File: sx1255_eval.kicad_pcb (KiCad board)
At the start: 2 copper layers, 26 parts, among them IC1 SX1255, J1 EXT_CLK_IN, J2 TX_SMA, J3 RX_SMA, J4 CONN

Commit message: WIP PCB layout
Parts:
- moved R9 44.7 mm to (159.5, 90.9), turned to 180 degrees
- moved R8 44.2 mm to (159.5, 89.4), turned to 180 degrees
- moved R7 43.6 mm to (159.5, 87.9), turned to 180 degrees
- moved R2 36.1 mm to (148.8, 96.5), turned to -90 degrees
- moved R6 34.3 mm to (154.9, 96.5), turned to -90 degrees
- moved R1 33.4 mm to (147.3, 96.5), turned to -90 degrees
- moved R5 32.0 mm to (153.4, 96.5), turned to -90 degrees
- moved R4 29.8 mm to (151.9, 96.5), turned to -90 degrees
- moved R3 27.7 mm to (150.4, 96.5), turned to -90 degrees
- moved J1 19.2 mm to (142.5, 90.9), turned to 90 degrees
- moved L1 12.1 mm to (129.8, 115.3)
- moved L2 8.03 mm to (126.5, 115.3)
- moved J4 4.61 mm to (168.2, 82.5)
- moved IC1 0.67 mm to (150.9, 89.2)
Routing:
- net CK_OUT: track 0.00 -> 57.2 mm
- net CK_IN: track 0.00 -> 51.9 mm
- net Q_IN: track 0.00 -> 46.6 mm
- net I_IN: track 0.00 -> 41.1 mm
- net Q_OUT: track 0.00 -> 35.8 mm
- net I_OUT: track 0.00 -> 30.4 mm
- net DIO3: track 0.00 -> 19.2 mm
- net DIO2: track 0.00 -> 17.3 mm
- net DIO1: track 0.00 -> 15.9 mm
- net DIO0: track 0.00 -> 15.0 mm
- net ~{CS}: track 0.00 -> 14.2 mm
- net Net-(IC1-MOSI): track 0.00 -> 6.24 mm
- net SCK: track 0.00 -> 6.09 mm
- net Net-(IC1-MISO): track 0.00 -> 5.81 mm
- net MISO: track 0.00 -> 5.66 mm
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
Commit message: WIP PCB
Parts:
- added C1: 10n, Capacitor_SMD:C_0603_1608Metric, F.Cu at (142.7, 87.1)
- added C6: 100n, Capacitor_SMD:C_0603_1608Metric, F.Cu at (159.5, 94.0)
- moved C3 45.9 mm to (159.5, 92.5)
- moved C12 43.4 mm to (154.7, 82.0), turned to 90 degrees
- moved L2 41.7 mm to (151.6, 82.0), turned to -90 degrees
- moved C5 40.9 mm to (145.5, 82.0), turned to 90 degrees
- moved L1 40.7 mm to (153.2, 82.0), turned to -90 degrees
- moved C7 39.2 mm to (142.7, 84.1), turned to 180 degrees
- moved C9 38.5 mm to (142.7, 90.2), turned to 180 degrees
- moved C11 38.2 mm to (150.1, 82.0), turned to 90 degrees
- moved C8 37.8 mm to (142.7, 88.6), turned to 180 degrees
- moved C2 37.6 mm to (147.1, 82.0), turned to 90 degrees
- moved C10 35.5 mm to (148.6, 82.0), turned to 90 degrees
- moved C4 34.9 mm to (142.7, 85.6), turned to 180 degrees
- moved J3 33.7 mm to (156.2, 71.0), turned to 180 degrees
- moved J2 28.8 mm to (141.0, 71.0), turned to 180 degrees
- moved J1 4.60 mm to (143.0, 95.5), turned to 180 degrees
- renumbered C8 to C10, C9 to C11, C10 to C12, C1 to C2, C2 to C3, C3 to C4, C4 to C5, C5 to C7, C6 to C8, C7 to C9
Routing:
- net RST: track 0.00 -> 69.1 mm
- net +3V3: track 0.00 -> 56.4 mm, vias 0 -> 4
- net Net-(J2-In): track 0.00 -> 13.6 mm
- net Net-(J3-In): track 0.00 -> 12.3 mm
- net EXT_CLK: track 0.00 -> 7.13 mm
- net Net-(IC1-VR_PA): track 0.00 -> 6.32 mm
- net Net-(IC1-RFI): track 0.00 -> 5.52 mm
- net Net-(IC1-VR_DIG): track 0.00 -> 5.18 mm
- net Net-(IC1-VR_ANAI): track 0.00 -> 4.96 mm
- net Net-(IC1-VR_ANA2): track 0.00 -> 4.86 mm
- net Net-(IC1-RFO_P): track 0.00 -> 4.64 mm
- net Net-(IC1-RFO_N): track 0.00 -> 4.22 mm
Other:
- board outline added: 43 x 34 mm

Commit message: PCB cleanup
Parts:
- moved R7 3.31 mm to (159.3, 91.2)
- moved C3 3.31 mm to (159.3, 95.8)
- moved C6 3.31 mm to (159.3, 97.3)
- moved R8 3.31 mm to (159.3, 92.7)
- moved R9 3.31 mm to (159.3, 94.2)
- moved J4 3.05 mm to (168.2, 85.6)
- moved J2 3.03 mm to (144.0, 71.0)
- moved J3 0.18 mm to (156.0, 71.0)
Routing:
- net DIO3: track 19.2 -> 16.3 mm
- net DIO2: track 17.3 -> 15.4 mm
- net RST: track 69.1 -> 67.4 mm
- net CK_OUT: track 57.2 -> 55.4 mm
- net CK_IN: track 51.9 -> 50.1 mm
- net Q_IN: track 46.6 -> 44.8 mm
- net I_IN: track 41.1 -> 39.3 mm
- net Q_OUT: track 35.8 -> 34.0 mm
- net I_OUT: track 30.4 -> 28.7 mm
- net +3V3: track 56.4 -> 54.7 mm
- net Net-(J2-In): track 13.6 -> 12.1 mm
- net DIO1: track 15.9 -> 14.6 mm
- net ~{CS}: track 14.2 -> 12.9 mm
- net DIO0: track 15.0 -> 13.7 mm
- net Net-(IC1-SCK): track 5.39 -> 6.54 mm
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- added copper zone on B.Cu, net GND
- added copper zone on F.Cu, net GND
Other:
- board text added: "3V3"
- board text added: "CK_IN"
- board text added: "CK_OUT"
- board text added: "EXT REF"
- board text added: "GND"
- board text added: "IO0"
- board text added: "IO1"
- board text added: "IO2"
- board text added: "IO3"
- board text added: "I_IN"
- board text added: "MISO"
- board text added: "MOSI"
- board text added: "Q_IN"
- board text added: "Q_OUT"
- board text added: "RST"
- board text added: "RX"
- board text added: "SCK"
- board text added: "SX1255 Minimalistic Evaluation Board"
- board text added: "TX"
- board text added: "Wojciech SP5WWP M17 Project 2023"
- board text added: "~{CS}"

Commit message: PMOD
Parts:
- added J5: PMOD, Connector_PinHeader_2.54mm:PinHeader_2x06_P2.54mm_Horizontal, F.Cu at (165.6, 94.5)
- added JP1: EXT_CLK_SRC, Connector_PinHeader_2.54mm:PinHeader_1x03_P2.54mm_Vertical, F.Cu at (145.5, 107.2)
- added REF**: OSHW-Logo2_7.3x6mm_SilkScreen, Symbol:OSHW-Logo2_7.3x6mm_SilkScreen, F.Cu at (140.7, 96.3)
- J1: footprint Connector_Coaxial:U.FL_Molex_MCRF_73412-0110_Vertical -> Connector_Coaxial:SMA_Samtec_SMA-J-P-X-ST-EM1_EdgeMount
- J4: value CONN -> PMOD; footprint Connector_PinHeader_2.54mm:PinHeader_2x09_P2.54mm_Vertical_SMD -> Connector_PinHeader_2.54mm:PinHeader_2x06_P2.54mm_Horizontal
- moved J3 22.5 mm to (134.1, 76.0), turned to -90 degrees
- moved J2 21.0 mm to (134.1, 89.5), turned to -90 degrees
- moved J4 14.2 mm to (165.6, 71.6)
- moved J1 11.6 mm to (134.1, 103.0), turned to -90 degrees
- moved C3 2.90 mm to (156.5, 96.5), turned to -90 degrees
- moved R7 2.54 mm to (159.3, 88.6)
- moved R8 2.54 mm to (159.3, 90.2)
- moved R9 2.54 mm to (159.3, 91.7)
- moved C7 1.48 mm to (158.0, 96.5), turned to -90 degrees
- renumbered C7 to C6, C6 to C7
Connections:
- net Net-(J2-In) renamed /RF_OUT
- net Net-(J3-In) renamed /RF_IN
- J1 pad 1: EXT_CLK -> EXT_CLK_B
- J4 pad 10: I_IN -> MISO
- J4 pad 11: ~{CS} -> MOSI
- J4 pad 12: Q_OUT -> SCK
- J4 pad 2: RST -> +3V3
- J4 pad 3: DIO3 -> GND
- J4 pad 4: CK_OUT -> GND
- J4 pad 5: DIO2 -> DIO3
- J4 pad 6: CK_IN -> DIO2
- J4 pad 8: Q_IN -> DIO0
- J4 pad 9: DIO0 -> ~{CS}
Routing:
- net RST: track 67.4 -> 31.1 mm
- net CK_OUT: track 55.4 -> 25.5 mm
- net CK_IN: track 50.1 -> 20.3 mm
- net Q_IN: track 44.8 -> 21.4 mm
- net I_IN: track 39.3 -> 16.1 mm
- net EXT_CLK_A: track 0.00 -> 18.6 mm
- net +3V3: track 54.7 -> 72.2 mm, vias 4 -> 3
- net Q_OUT: track 34.0 -> 17.1 mm
- net I_OUT: track 28.7 -> 12.0 mm
- net EXT_CLK_B: track 0.00 -> 13.4 mm
- net GND: track 0.00 -> 12.2 mm, vias 69 -> 186
- net /RF_OUT: track 12.1 -> 24.2 mm
- net EXT_CLK: track 7.13 -> 18.8 mm
- net /RF_IN: track 12.0 -> 21.1 mm
- net MISO: track 5.77 -> 12.7 mm
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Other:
- board size 43 x 34 mm -> 40 x 41 mm
- board text added: "EXT REF SEL"
- board text added: "I_OUT"
- board text added: "OUT"
- board text added: "REF"
- board text added: "SX1255 Minimalistic Evaluation Board M17 Project, December 2023 Wojciech SP5WWP"
- board text removed: "3V3"
- board text removed: "CK_OUT"
- board text removed: "GND"
- board text removed: "SX1255 Minimalistic Evaluation Board"
- board text removed: "Wojciech SP5WWP M17 Project 2023"

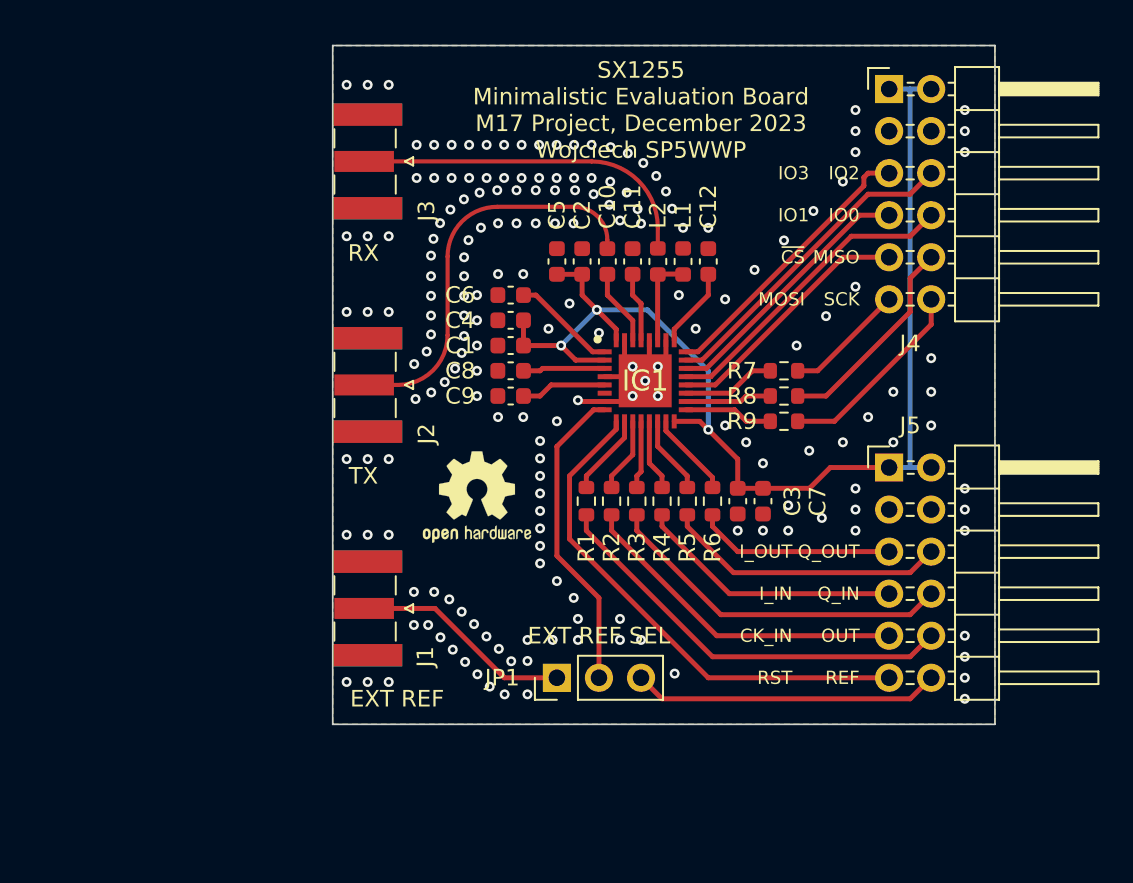
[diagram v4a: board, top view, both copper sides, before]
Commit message: changed PCB orientation
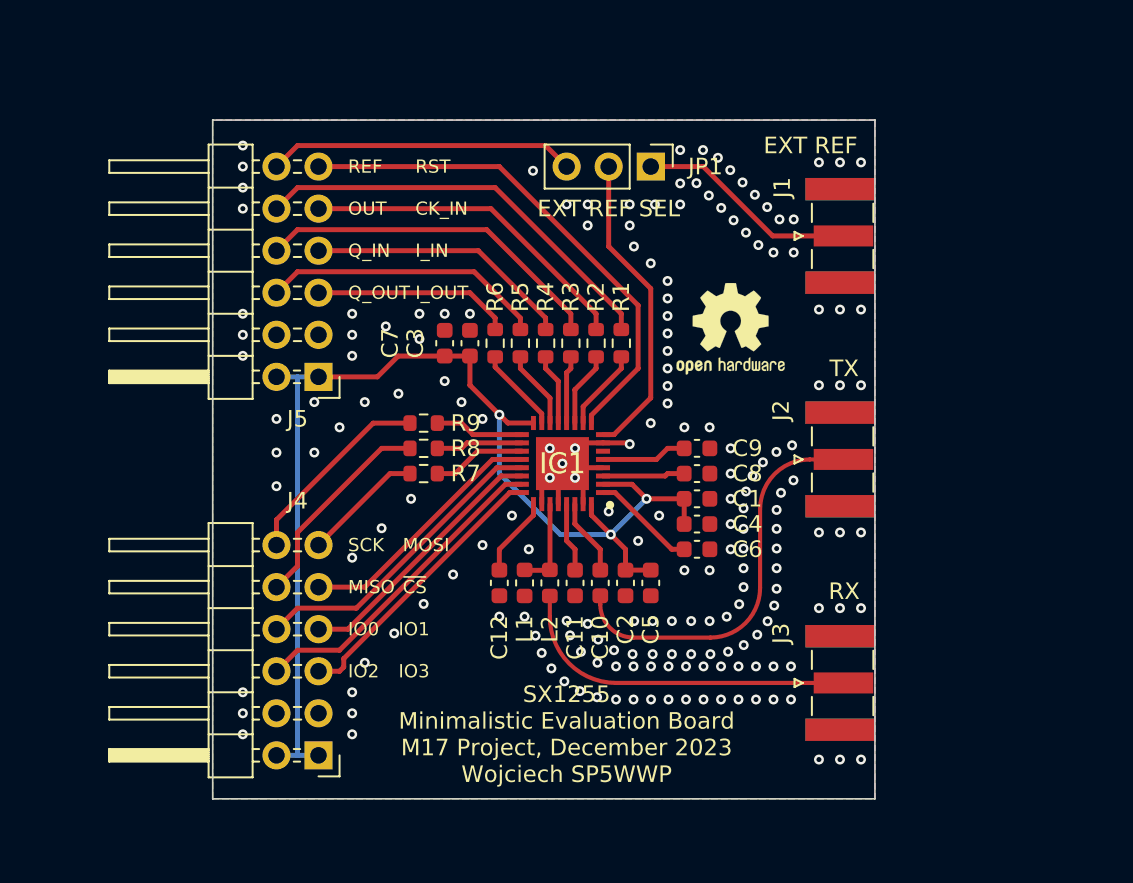
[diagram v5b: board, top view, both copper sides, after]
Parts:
- moved J4 53.0 mm to (131.1, 111.9), turned to 180 degrees
- moved J3 42.5 mm to (162.7, 107.5), turned to 90 degrees
- moved J1 36.4 mm to (162.7, 80.5), turned to 90 degrees
- moved J5 34.9 mm to (131.1, 89.0), turned to 180 degrees
- moved JP1 31.4 mm to (151.2, 76.3), turned to -90 degrees
- moved J2 28.9 mm to (162.7, 94.0), turned to 90 degrees
- moved C12 23.2 mm to (142.1, 101.5), turned to -90 degrees
- moved R7 22.6 mm to (137.5, 94.9), turned to 0 degrees
- moved R8 22.0 mm to (137.5, 93.3), turned to 0 degrees
- moved R9 21.8 mm to (137.5, 91.8), turned to 0 degrees
- moved L1 21.6 mm to (143.6, 101.5), turned to 90 degrees
- moved C7 21.5 mm to (138.8, 87.0), turned to 90 degrees
- moved L2 20.5 mm to (145.1, 101.5), turned to 90 degrees
- moved C5 20.2 mm to (151.2, 101.5), turned to -90 degrees
- moved C11 19.7 mm to (146.6, 101.5), turned to -90 degrees
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
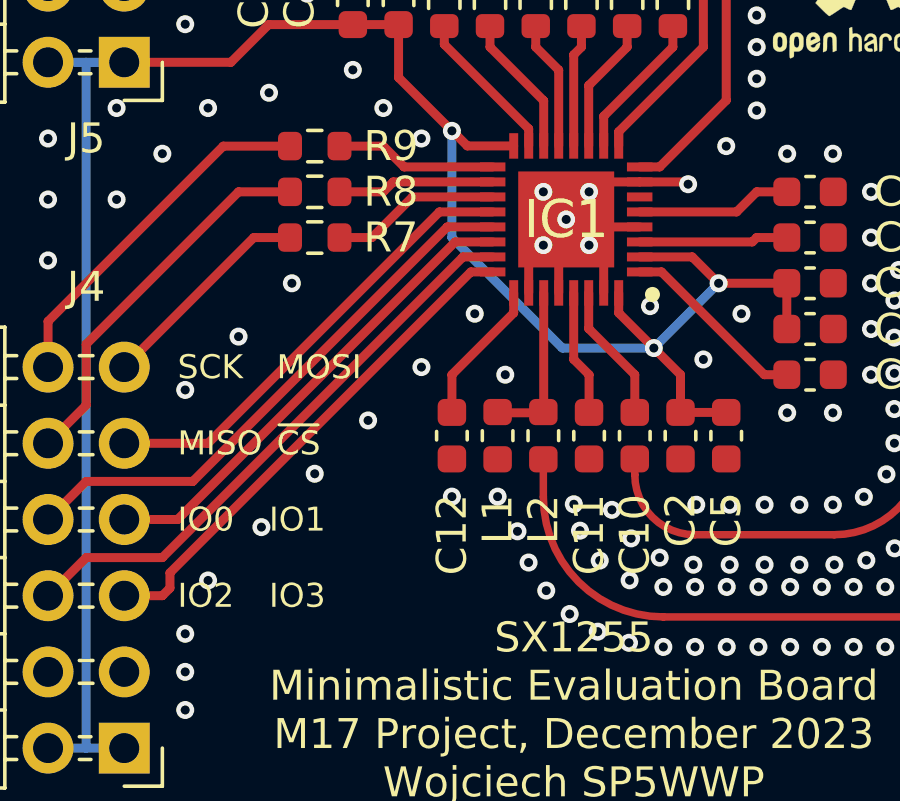
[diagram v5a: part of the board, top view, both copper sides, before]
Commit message: PN update, gerbers
minor silkscreen tweaks
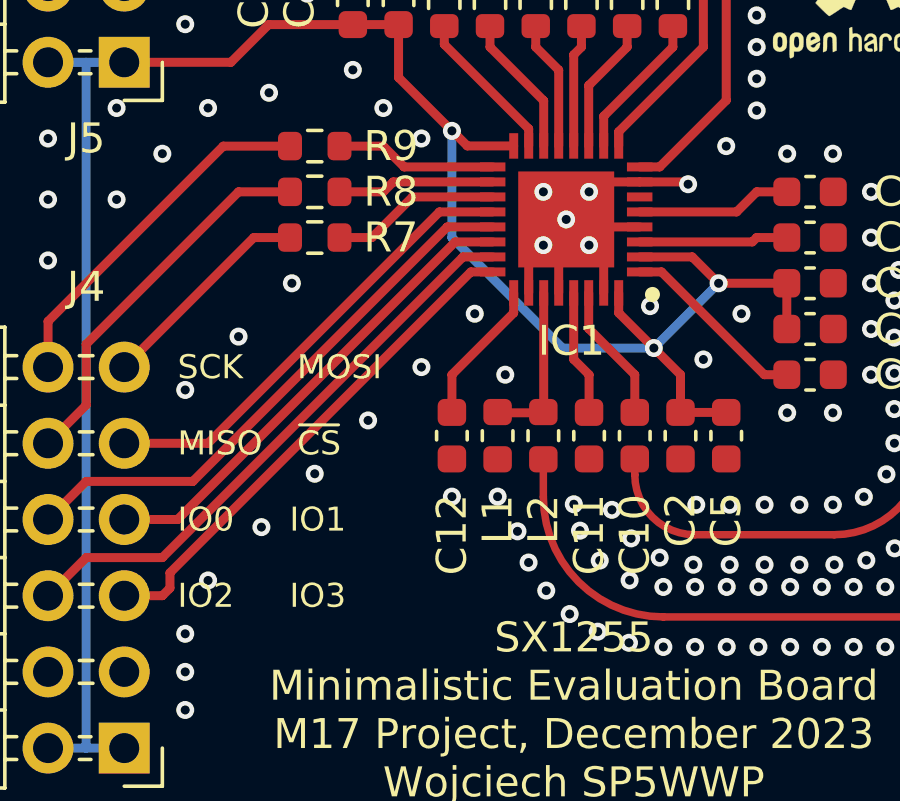
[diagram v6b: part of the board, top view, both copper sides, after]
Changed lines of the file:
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@@
       (plot_on_all_layers_selection 0x0000000_00000000)
       (disableapertmacros false)
-      (usegerberextensions false)
-      (usegerberattributes true)
-      (usegerberadvancedattributes true)
-      (creategerberjobfile true)
+      (usegerberextensions true)
+      (usegerberattributes false)
+      (usegerberadvancedattributes false)
+      (creategerberjobfile false)
       (dashed_line_dash_ratio 12.000000)
       (dashed_line_gap_ratio 3.000000)
@@
       (psa4output false)
       (plotreference true)
-      (plotvalue true)
+      (plotvalue false)
       (plotinvisibletext false)
       (sketchpadsonfab false)
-      (subtractmaskfromsilk false)
+      (subtractmaskfromsilk true)
       (outputformat 1)
       (mirror false)
-      (drillshape 1)
+      (drillshape 0)
       (scaleselection 1)
-      (outputdirectory "")
+      (outputdirectory "fab/")
     )
   )
@@
     (property "ki_description" "RF Transceiver RF Front End Transceiver")
     (attr smd)
-    (fp_text reference "IC1" (at 0 0) (layer "F.SilkS")
-        (effects (font (size 1.27 1.27) (thickness 0.254)))
+    (fp_text reference "IC1" (at -0.174 -4.048) (layer "F.SilkS")
+        (effects (font (size 1 1) (thickness 0.15)))
     )
     (fp_text value "SX1255" (at 0 0) (layer "F.SilkS") hide
@@
     (effects (font (size 0.8 0.8) (thickness 0.1)) (justify left))
   )
-  (gr_text "MOSI" (at 136.224 99.172) (layer "F.SilkS")
+  (gr_text "MOSI" (at 136.906 99.172) (layer "F.SilkS")
     (effects (font (size 0.8 0.8) (thickness 0.1)) (justify left))
   )
@@
     (effects (font (size 0.8 0.8) (thickness 0.1)) (justify left))
   )
-  (gr_text "IO3" (at 135.97 106.792) (layer "F.SilkS")
+  (gr_text "IO3" (at 136.652 106.792) (layer "F.SilkS")
     (effects (font (size 0.8 0.8) (thickness 0.1)) (justify left))
   )
@@
     (effects (font (size 0.8 0.8) (thickness 0.1)) (justify left))
   )
-  (gr_text "IO1" (at 135.97 104.252) (layer "F.SilkS")
+  (gr_text "IO1" (at 136.652 104.252) (layer "F.SilkS")
     (effects (font (size 0.8 0.8) (thickness 0.1)) (justify left))
   )
-  (gr_text "~{CS}" (at 136.224 101.712) (layer "F.SilkS")
+  (gr_text "~{CS}" (at 136.906 101.712) (layer "F.SilkS")
     (effects (font (size 0.8 0.8) (thickness 0.1)) (justify left))
   )
